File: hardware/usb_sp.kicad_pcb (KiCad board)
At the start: 4 copper layers, 38.1 x 59.7 mm, 48 parts, among them U1 CH32V203C8U6, U10 SN74LVC1G32DBVR, U2 ZD24C02B-MAGMT, U3 32.768kHz, U4 KH-TYPE-C-16P, U5 SD101CWS, U6 CH572D, U7 HX_JN1_27-2X5P_ZZ_H4_9, U8 HX_JN1_27-2X5P_ZZ_H4_9, U9 SN74LVC1G32DBVR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

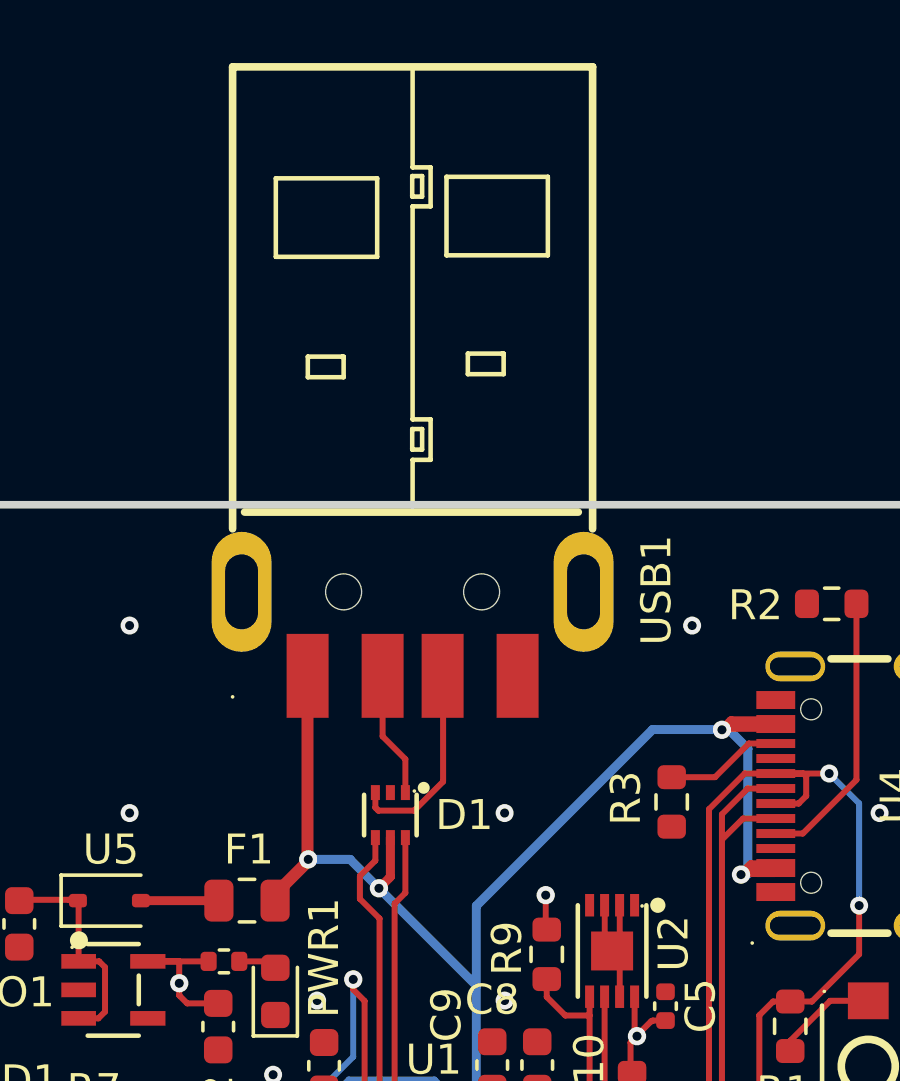
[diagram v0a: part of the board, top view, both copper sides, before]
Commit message: refactor: minor schematic visual changes
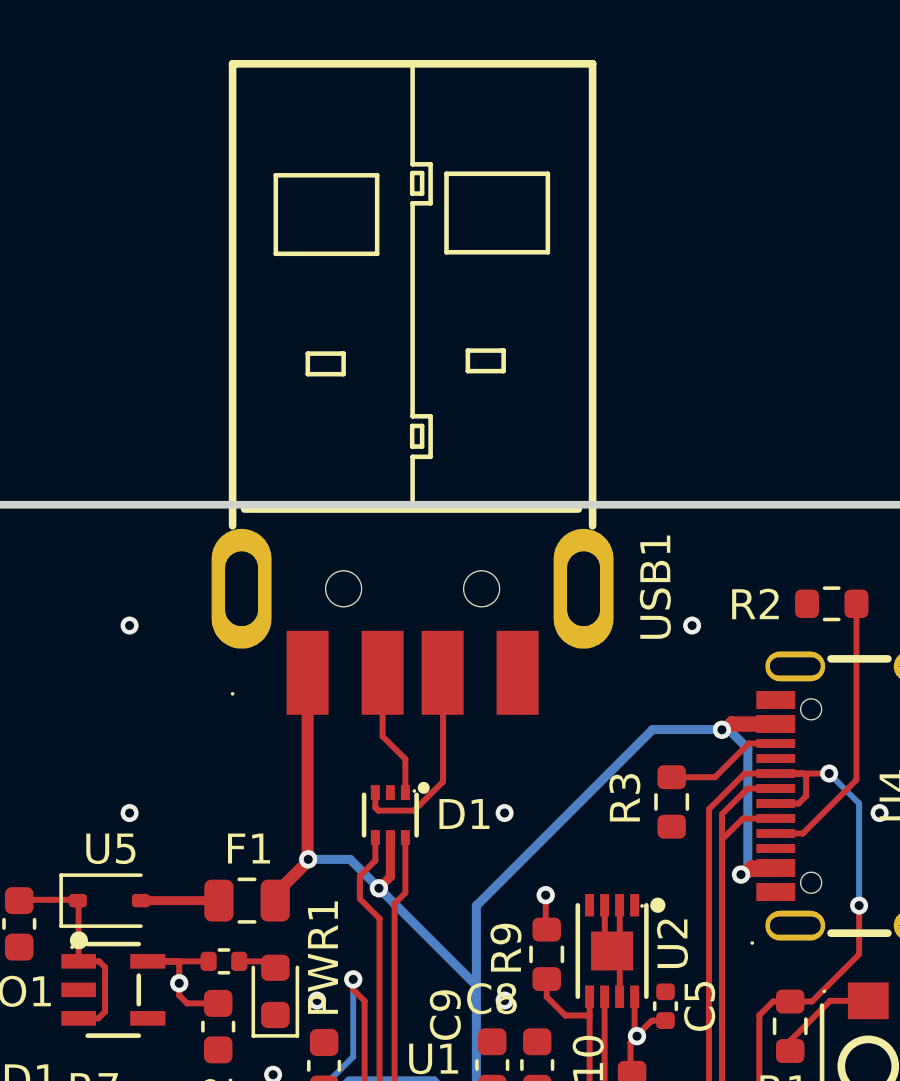
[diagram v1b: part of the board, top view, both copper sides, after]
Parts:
- moved USB1 0.10 mm to (145.9, 71.0)
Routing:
- net /CH32V203/D+: track 6.38 -> 7.35 mm
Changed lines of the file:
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@@
 			(net 17 "unconnected-(U1-PC13{slash}TAMPER_RTC-Pad2)")
 			(pinfunction "PC13/TAMPER_RTC")
-			(pintype "unspecified")
+			(pintype "unspecified+no_connect")
 		)
 		(pad "3" smd rect
@@
 			(net 14 "unconnected-(U1-PA0{slash}WKUP{slash}ADC0-Pad10)")
 			(pinfunction "PA0/WKUP/ADC0")
-			(pintype "unspecified")
+			(pintype "unspecified+no_connect")
 		)
 		(pad "11" smd rect
@@
 			(net 19 "unconnected-(U1-PA1{slash}ADC1-Pad11)")
 			(pinfunction "PA1/ADC1")
-			(pintype "unspecified")
+			(pintype "unspecified+no_connect")
 		)
 		(pad "12" smd rect
@@
 			(net 20 "unconnected-(U1-PA2{slash}ADC2-Pad12)")
 			(pinfunction "PA2/ADC2")
-			(pintype "unspecified")
+			(pintype "unspecified+no_connect")
 		)
 		(pad "13" smd rect
@@
 			(net 9 "unconnected-(U1-PA3{slash}ADC3-Pad13)")
 			(pinfunction "PA3/ADC3")
-			(pintype "unspecified")
+			(pintype "unspecified+no_connect")
 		)
 		(pad "14" smd rect
@@
 			(net 22 "unconnected-(U1-PA4{slash}ADC4-Pad14)")
 			(pinfunction "PA4/ADC4")
-			(pintype "unspecified")
+			(pintype "unspecified+no_connect")
 		)
 		(pad "15" smd rect
@@
 			(net 11 "unconnected-(U1-PB0{slash}ADC8-Pad18)")
 			(pinfunction "PB0/ADC8")
-			(pintype "unspecified")
+			(pintype "unspecified+no_connect")
 		)
 		(pad "19" smd rect
@@
 			(net 13 "unconnected-(U1-PB1{slash}ADC9-Pad19)")
 			(pinfunction "PB1/ADC9")
-			(pintype "unspecified")
+			(pintype "unspecified+no_connect")
 		)
 		(pad "20" smd rect
@@
 			(net 8 "unconnected-(U1-PB12-Pad25)")
 			(pinfunction "PB12")
-			(pintype "unspecified")
+			(pintype "unspecified+no_connect")
 		)
 		(pad "26" smd rect
@@
 			(net 21 "unconnected-(U1-PB13-Pad26)")
 			(pinfunction "PB13")
-			(pintype "unspecified")
+			(pintype "unspecified+no_connect")
 		)
 		(pad "27" smd rect
@@
 			(net 25 "unconnected-(U1-PB14-Pad27)")
 			(pinfunction "PB14")
-			(pintype "unspecified")
+			(pintype "unspecified+no_connect")
 		)
 		(pad "28" smd rect
@@
 			(net 15 "unconnected-(U1-PB15-Pad28)")
 			(pinfunction "PB15")
-			(pintype "unspecified")
+			(pintype "unspecified+no_connect")
 		)
 		(pad "29" smd rect
@@
 			(net 10 "unconnected-(U1-PA8-Pad29)")
 			(pinfunction "PA8")
-			(pintype "unspecified")
+			(pintype "unspecified+no_connect")
 		)
 		(pad "30" smd rect
@@
 			(net 18 "unconnected-(U1-PA15-Pad38)")
 			(pinfunction "PA15")
-			(pintype "unspecified")
+			(pintype "unspecified+no_connect")
 		)
 		(pad "39" smd rect
@@
 			(net 24 "unconnected-(U1-PB3-Pad39)")
 			(pinfunction "PB3")
-			(pintype "unspecified")
+			(pintype "unspecified+no_connect")
 		)
 		(pad "40" smd rect
@@
 			(net 12 "unconnected-(U1-PB4-Pad40)")
 			(pinfunction "PB4")
-			(pintype "unspecified")
+			(pintype "unspecified+no_connect")
 		)
 		(pad "41" smd rect
@@
 			(net 16 "unconnected-(U1-PB5-Pad41)")
 			(pinfunction "PB5")
-			(pintype "unspecified")
+			(pintype "unspecified+no_connect")
 		)
 		(pad "42" smd rect
@@
 	(footprint "usb_sp_fp:USB-A-SMD_917-181A102ES60200"
 		(layer "F.Cu")
-		(at 145.879523 71.058335 90)
+		(at 145.879523 70.956735 90)
 		(descr "USB-A-SMD_917-181A102ES60200 footprint")
 		(tags "USB-A-SMD_917-181A102ES60200 footprint C46394")
@@
 	)
 	(segment
-		(start 146.895523 75.984809)
-		(end 145.929523 76.950809)
+		(start 145.929523 76.950809)
+		(end 144.738727 76.950809)
 		(width 0.2)
 		(layer "F.Cu")
@@
 	)
 	(segment
-		(start 146.895523 72.855335)
+		(start 146.895523 72.372735)
 		(end 146.895523 75.984809)
 		(width 0.2)
@@
 	)
 	(segment
-		(start 144.638523 76.850605)
-		(end 144.638523 76.348745)
+		(start 146.900523 72.860335)
+		(end 146.879523 72.839335)
 		(width 0.2)
 		(layer "F.Cu")
@@
 	)
 	(segment
-		(start 145.929523 76.950809)
-		(end 144.738727 76.950809)
+		(start 146.879523 72.356735)
+		(end 146.895523 72.372735)
 		(width 0.2)
 		(layer "F.Cu")
@@
 	)
 	(segment
-		(start 146.900523 72.860335)
-		(end 146.879523 72.839335)
+		(start 146.879523 72.839335)
+		(end 146.879523 72.356735)
+		(width 0.2)
+		(layer "F.Cu")
+		(net 41)
+	)
+	(segment
+		(start 144.638523 76.850605)
+		(end 144.638523 76.348745)
 		(width 0.2)
 		(layer "F.Cu")
@@
 	)
 	(segment
-		(start 146.879523 72.839335)
-		(end 146.895523 72.855335)
+		(start 146.895523 75.984809)
+		(end 145.929523 76.950809)
 		(width 0.2)
 		(layer "F.Cu")
@@
 	)
 	(segment
-		(start 145.638523 76.348745)
-		(end 145.638523 75.234809)
+		(start 144.879523 74.475809)
+		(end 144.879523 72.356735)
 		(width 0.2)
 		(layer "F.Cu")
@@
 	)
 	(segment
-		(start 144.879523 74.475809)
-		(end 144.879523 72.839335)
+		(start 145.638523 76.348745)
+		(end 145.638523 75.234809)
 		(width 0.2)
 		(layer "F.Cu")
@@
 	)
 	(segment
-		(start 142.37965 72.839335)
-		(end 142.37615 72.842835)
+		(start 142.37965 78.650682)
+		(end 141.259523 79.770809)
+		(width 0.4)
+		(layer "F.Cu")
+		(net 71)
+	)
+	(segment
+		(start 141.259523 79.770809)
+		(end 141.259523 79.950809)
 		(width 0.4)
 		(layer "F.Cu")
@@
 	)
 	(segment
-		(start 142.37615 78.654182)
-		(end 141.259523 79.770809)
-		(width 0.4)
-		(layer "F.Cu")
-		(net 71)
-	)
-	(segment
 		(start 142.099323 119.023826)
 		(end 142.651306 119.575809)
@@
 	)
 	(segment
-		(start 160.484523 116.615009)
-		(end 160.484523 115.395809)
-		(width 0.3)
+		(start 142.37965 72.839335)
+		(end 142.37965 78.650682)
+		(width 0.4)
 		(layer "F.Cu")
 		(net 71)
 	)
 	(segment
-		(start 141.259523 79.770809)
-		(end 141.259523 79.950809)
-		(width 0.4)
+		(start 160.484523 116.615009)
+		(end 160.484523 115.395809)
+		(width 0.3)
 		(layer "F.Cu")
 		(net 71)
@@
 		(layer "F.Cu")
 		(net 71)
-	)
-	(segment
-		(start 142.37615 72.842835)
-		(end 142.37615 78.654182)
-		(width 0.4)
-		(layer "F.Cu")
-		(net 71)

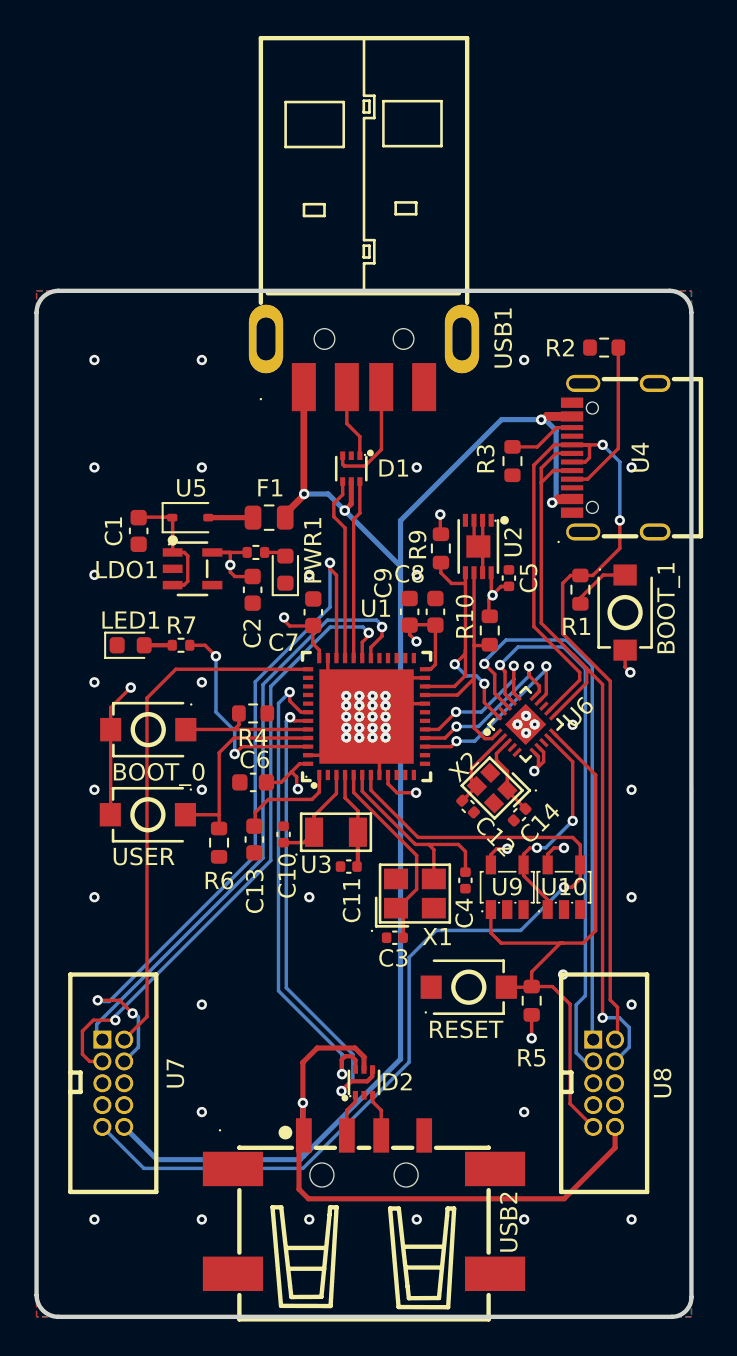
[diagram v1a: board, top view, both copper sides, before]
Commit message: fix: add missing cs line to spi bus
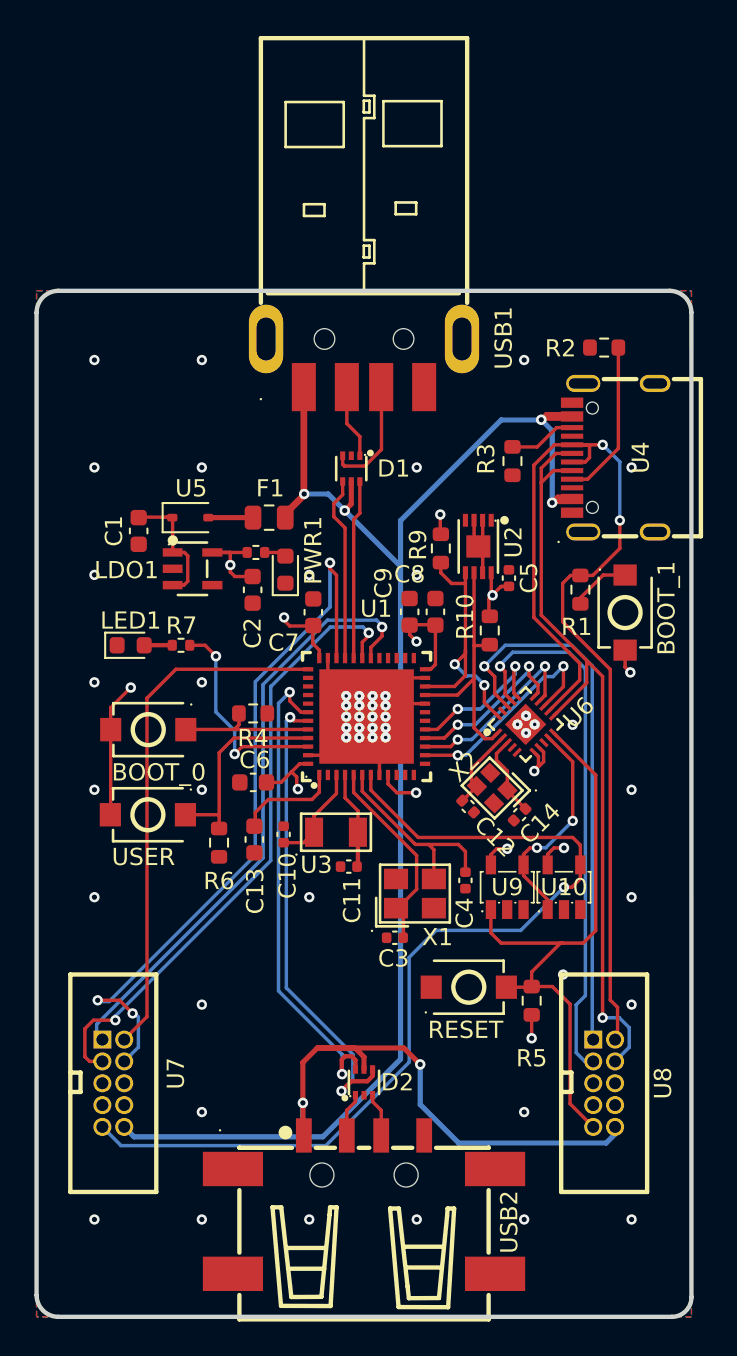
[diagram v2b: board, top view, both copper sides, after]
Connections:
- U1 pad 14: unconnected-(U1-PA4/ADC4-Pad14) -> /CH32V203/SPI_CS
- U6 pad 13: unconnected-(U6-PA4_/SCS/P_WM4/TM_R2-Pad13) -> /CH32V203/SPI_CS
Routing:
- net /CH32V203/SPI_CS: track 0.00 -> 13.2 mm, vias 0 -> 2
- net VBUS: track 126.2 -> 121.1 mm, vias 5 -> 6
- net /CH32V203/RST_CH32: track 55.7 -> 54.6 mm
- net /CH572D/SWDIO: track 46.5 -> 45.8 mm
